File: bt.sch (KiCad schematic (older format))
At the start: 3 parts, among them J5 RN52_BREAKOUT, P1 CONN_01X06

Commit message: Add a line in module and use a smaller jack.
Lots of changes:
Added a line in. This requires another audio switch, so that's added to
the audio switch module.
Also, since I'm using two jacks, I chose a smaller jack module. This
needed a new footprint, and a new 3d model. The footprint is trickier,
since it really needed slots, which OSH won't guarantee. I've given it a
unique footprint to try to optimize the pad size around the edges of the
pins.
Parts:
- renumbered C4 to C3, J5 to J6
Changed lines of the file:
@@
 $Descr USLetter 11000 8500
 encoding utf-8
-Sheet 6 8
+Sheet 6 10
 Title "Blubaru"
 Date "2017-02-28"
@@
 $EndDescr
 $Comp
-L RN52_BREAKOUT J5
+L RN52_BREAKOUT J6
 U 1 1 589AA2F8
 P 5100 2950
-F 0 "J5" H 5100 850 60  0000 C CNN
+F 0 "J6" H 5100 850 60  0000 C CNN
 F 1 "RN52_BREAKOUT" H 5100 2950 60  0000 C CNN
 F 2 "blubaru:RN52_Breakout" H 5100 2950 60  0001 C CNN
@@
 NoConn ~ 5800 3950
 $Comp
-L C C4
+L C C3
 U 1 1 589BA198
 P 4250 5150
-F 0 "C4" H 4275 5250 50  0000 L CNN
+F 0 "C3" H 4275 5250 50  0000 L CNN
 F 1 "0.1uF" H 4275 5050 50  0000 L CNN
 F 2 "blubaru:C_Disc_D4.0mm_W2.6mm_P2.50mm" H 4288 5000 50  0001 C CNN
@@
 $EndSheet
 Text HLabel 8150 3050 2    60   Output ~ 0
-LineOutL
+BT_L
 Text HLabel 8150 3150 2    60   Output ~ 0
-LineOutR
+BT_R
 Wire Wire Line
 	7800 3050 8150 3050

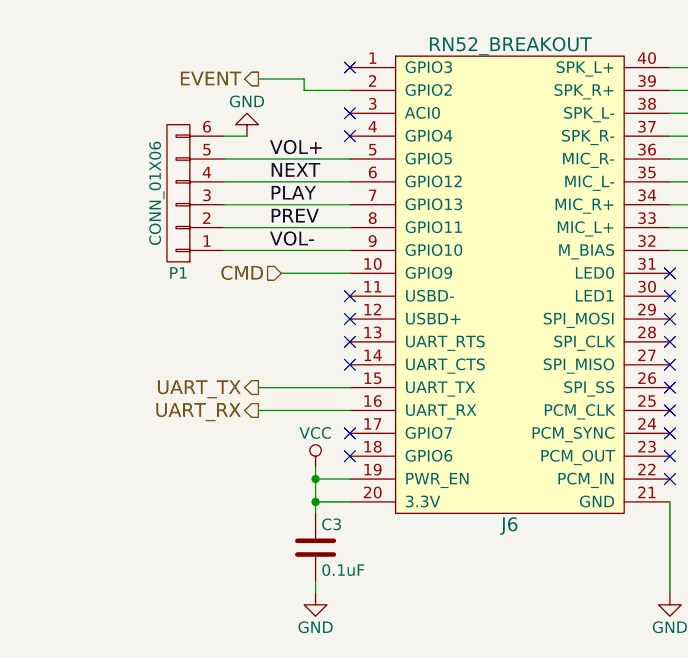
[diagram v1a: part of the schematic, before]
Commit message: Major update to use Atmel ATTINY4313
Replace Pro Micro as microcontroller. Mostly contianed within the
control sheet.
Moved LEDs all onto control sheet.
Updated a few capacitors.
Added a reset switch. Still need to decide part.
Updated a few capacitor models for 4.0.7
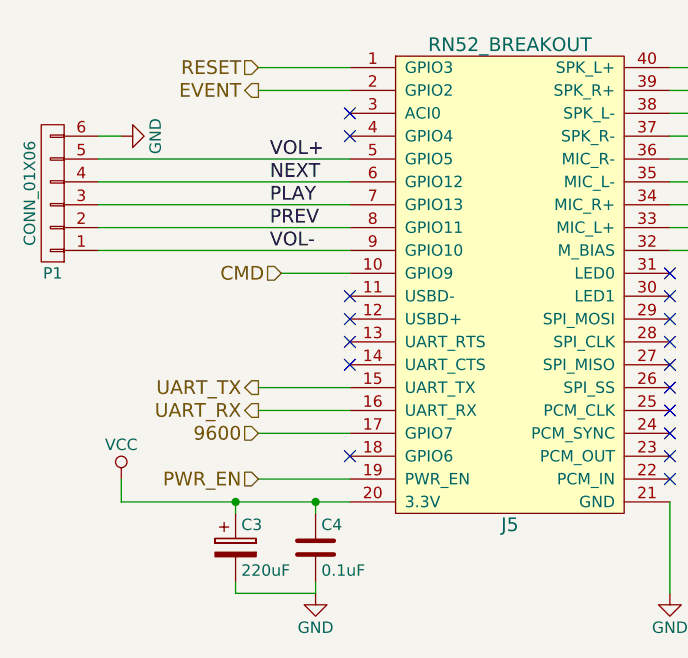
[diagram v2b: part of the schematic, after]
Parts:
- added C3: 220uF, blubaru:CP_Radial_D6.3mm_P2.50mm, symbol CP
- renumbered C3 to C4, J6 to J5
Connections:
- net GND: now also C3.2
- net VCC: now also C3.1; no longer J5.19 (PWR_EN)
- net RESET: now reaches J5.1 (GPIO3)
- net 9600: now reaches J5.17 (GPIO7)
- new net PWR_EN: J5.19 (PWR_EN)
- no-connect marks 19 -> 17
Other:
- moved on the sheet: P1
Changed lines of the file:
@@
 $Descr USLetter 11000 8500
 encoding utf-8
-Sheet 6 10
+Sheet 5 10
 Title "Blubaru"
 Date "2017-02-28"
@@
 $EndDescr
 $Comp
-L RN52_BREAKOUT J6
+L RN52_BREAKOUT J5
 U 1 1 589AA2F8
 P 5100 2950
-F 0 "J6" H 5100 850 60  0000 C CNN
+F 0 "J5" H 5100 850 60  0000 C CNN
 F 1 "RN52_BREAKOUT" H 5100 2950 60  0000 C CNN
 F 2 "blubaru:RN52_Breakout" H 5100 2950 60  0001 C CNN
@@
 $EndComp
 $Comp
-L GND #PWR022
+L GND #PWR017
 U 1 1 589AA392
 P 5800 5350
-F 0 "#PWR022" H 5800 5100 50  0001 C CNN
+F 0 "#PWR017" H 5800 5100 50  0001 C CNN
 F 1 "GND" H 5800 5200 50  0000 C CNN
 F 2 "" H 5800 5350 50  0000 C CNN
@@
 $EndComp
 $Comp
-L VCC #PWR023
+L VCC #PWR018
 U 1 1 589AA3E5
-P 4250 4800
-F 0 "#PWR023" H 4250 4650 50  0001 C CNN
-F 1 "VCC" H 4250 4950 50  0000 C CNN
-F 2 "" H 4250 4800 50  0000 C CNN
-F 3 "" H 4250 4800 50  0000 C CNN
-	1    4250 4800
-	1    0    0    -1
-$EndComp
-NoConn ~ 4400 3050
+P 3400 4850
+F 0 "#PWR018" H 3400 4700 50  0001 C CNN
+F 1 "VCC" H 3400 5000 50  0000 C CNN
+F 2 "" H 3400 4850 50  0000 C CNN
+F 3 "" H 3400 4850 50  0000 C CNN
+	1    3400 4850
+	1    0    0    -1
+$EndComp
 NoConn ~ 4400 3250
 NoConn ~ 4400 3350
@@
 NoConn ~ 4400 4250
 NoConn ~ 4400 4350
-NoConn ~ 4400 4650
 NoConn ~ 4400 4750
 NoConn ~ 5800 4850
@@
 NoConn ~ 5800 3950
 $Comp
-L C C3
+L C C4
 U 1 1 589BA198
 P 4250 5150
-F 0 "C3" H 4275 5250 50  0000 L CNN
+F 0 "C4" H 4275 5250 50  0000 L CNN
 F 1 "0.1uF" H 4275 5050 50  0000 L CNN
 F 2 "blubaru:C_Disc_D4.0mm_W2.6mm_P2.50mm" H 4288 5000 50  0001 C CNN
@@
 $EndComp
 Wire Wire Line
-	3850 3450 4400 3450
-Wire Wire Line
-	3850 3550 4400 3550
-Wire Wire Line
-	3850 3650 4400 3650
-Wire Wire Line
-	3850 3750 4400 3750
-Wire Wire Line
-	3850 3850 4400 3850
+	3300 3450 4400 3450
+Wire Wire Line
+	3300 3550 4400 3550
+Wire Wire Line
+	3300 3650 4400 3650
+Wire Wire Line
+	3300 3750 4400 3750
+Wire Wire Line
+	3300 3850 4400 3850
 Wire Wire Line
 	5800 4950 5800 5350
@@
 L CONN_01X06 P1
 U 1 1 589E7B79
-P 3650 3600
-F 0 "P1" H 3650 3950 50  0000 C CNN
-F 1 "CONN_01X06" V 3750 3600 50  0000 C CNN
-F 2 "Pin_Headers:Pin_Header_Straight_1x06_Pitch2.54mm" H 3650 3600 50  0001 C CNN
-F 3 "" H 3650 3600 50  0000 C CNN
-	1    3650 3600
+P 3100 3600
+F 0 "P1" H 3100 3950 50  0000 C CNN
+F 1 "CONN_01X06" V 3200 3600 50  0000 C CNN
+F 2 "Pin_Headers:Pin_Header_Straight_1x06_Pitch2.54mm" H 3100 3600 50  0001 C CNN
+F 3 "" H 3100 3600 50  0000 C CNN
+	1    3100 3600
 	-1   0    0    1
 $EndComp
 $Comp
-L GND #PWR024
+L GND #PWR019
 U 1 1 589E813D
-P 3950 3350
-F 0 "#PWR024" H 3950 3100 50  0001 C CNN
-F 1 "GND" H 3950 3200 50  0000 C CNN
-F 2 "" H 3950 3350 50  0000 C CNN
-F 3 "" H 3950 3350 50  0000 C CNN
-	1    3950 3350
-	-1   0    0    1
-$EndComp
-Wire Wire Line
-	3850 3350 3950 3350
+P 3400 3350
+F 0 "#PWR019" H 3400 3100 50  0001 C CNN
+F 1 "GND" H 3400 3200 50  0000 C CNN
+F 2 "" H 3400 3350 50  0000 C CNN
+F 3 "" H 3400 3350 50  0000 C CNN
+	1    3400 3350
+	0    -1   -1   0
+$EndComp
 Wire Wire Line
 	5800 3050 6700 3050
@@
 Text HLabel 4100 3950 0    60   Input ~ 0
 CMD
-Text HLabel 4000 3100 0    60   Output ~ 0
+Text HLabel 4000 3150 0    60   Output ~ 0
 EVENT
-Wire Wire Line
-	4000 3100 4200 3100
-Wire Wire Line
-	4200 3100 4200 3150
-Wire Wire Line
-	4200 3150 4400 3150
 Wire Wire Line
 	4100 3950 4400 3950
@@
 F7 "R+" I L 6700 3150 60
 $EndSheet
-Wire Wire Line
-	4400 4850 4250 4850
-Wire Wire Line
-	4250 4800 4250 5000
-Connection ~ 4250 4850
 Connection ~ 4250 4950
 Wire Wire Line
-	4250 4950 4400 4950
-$Comp
-L GND #PWR025
+	3400 4950 4400 4950
+$Comp
+L GND #PWR020
 U 1 1 594F3947
 P 4250 5350
-F 0 "#PWR025" H 4250 5100 50  0001 C CNN
+F 0 "#PWR020" H 4250 5100 50  0001 C CNN
 F 1 "GND" H 4250 5200 50  0000 C CNN
 F 2 "" H 4250 5350 50  0001 C CNN
@@
 Wire Wire Line
 	4250 5300 4250 5350
+$Comp
+L CP C3
+U 1 1 59F2DEF7
+P 3900 5150
+F 0 "C3" H 3925 5250 50  0000 L CNN
+F 1 "220uF" H 3925 5050 50  0000 L CNN
+F 2 "blubaru:CP_Radial_D6.3mm_P2.50mm" H 3938 5000 50  0001 C CNN
+F 3 "http://www.nichicon.co.jp/english/products/pdfs/e-usw.pdf" H 3900 5150 50  0001 C CNN
+	1    3900 5150
+	1    0    0    -1
+$EndComp
+Wire Wire Line
+	3900 5000 3900 4950
+Wire Wire Line
+	3900 5300 3900 5350
+Wire Wire Line
+	3900 5350 4250 5350
+Wire Wire Line
+	3400 4850 3400 4950
+Connection ~ 3900 4950
+Wire Wire Line
+	3300 3350 3400 3350
+Wire Wire Line
+	4400 4650 4000 4650
+Wire Wire Line
+	4400 4850 4000 4850
+Wire Wire Line
+	4400 3150 4000 3150
+Wire Wire Line
+	4400 3050 4000 3050
+Text HLabel 4000 3050 0    60   Input ~ 0
+RESET
+Text HLabel 4000 4650 0    60   Input ~ 0
+9600
+Text HLabel 4000 4850 0    60   Input ~ 0
+PWR_EN
+Wire Wire Line
+	4250 4950 4250 5000
 $EndSCHEMATC

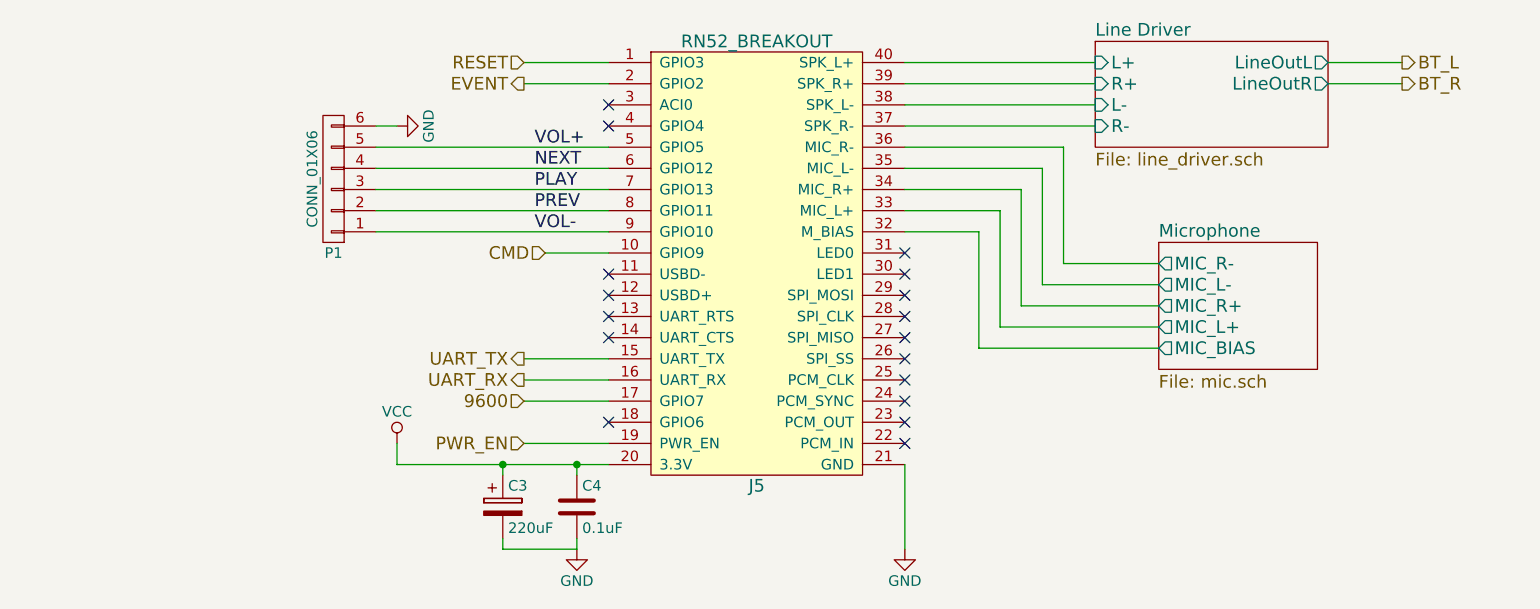
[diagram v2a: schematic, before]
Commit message: Add LEDs to BT module
These already exist on the breakout board, but they will be more visible
if I add resistors to the front panel. They can be removed if space is
limited and the case is translucent, but add them for now. In V2, there
won't be a breakout board, so adding them now makes the V1 to V2 fewer
changes.
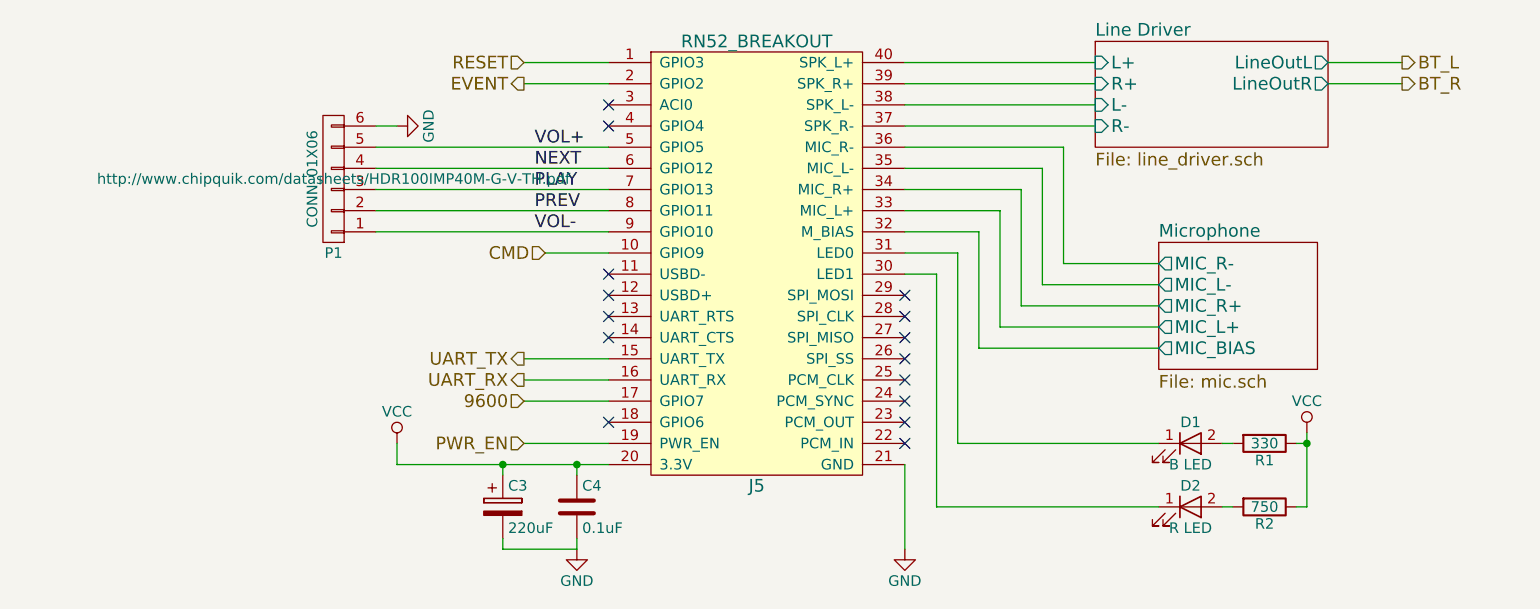
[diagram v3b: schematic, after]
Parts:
- added D1: B LED, LEDs:LED_D3.0mm_Horizontal_O1.27mm_Z6.0mm, symbol LED
- added D2: R LED, LEDs:LED_D3.0mm_Horizontal_O1.27mm_Z6.0mm, symbol LED
- added R1: 330, Resistors_THT:R_Axial_DIN0204_L3.6mm_D1.6mm_P5.08mm_Horizontal, symbol R
- added R2: 750, Resistors_THT:R_Axial_DIN0204_L3.6mm_D1.6mm_P5.08mm_Horizontal, symbol R
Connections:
- net VCC: now also R1.1, R2.1
- net at J5.30 (LED1): now also D2.1 (K)
- net at J5.31 (LED0): now also D1.1 (K)
- new net: D1.2 (A), R1.2
- new net: D2.2 (A), R2.2
- no-connect marks 17 -> 15
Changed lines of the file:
@@
 NoConn ~ 5800 4250
 NoConn ~ 5800 4150
-NoConn ~ 5800 4050
-NoConn ~ 5800 3950
 $Comp
 L C C4
@@
 F 1 "CONN_01X06" V 3200 3600 50  0000 C CNN
 F 2 "Pin_Headers:Pin_Header_Straight_1x06_Pitch2.54mm" H 3100 3600 50  0001 C CNN
-F 3 "" H 3100 3600 50  0000 C CNN
+F 3 "http://www.chipquik.com/datasheets/HDR100IMP40M-G-V-TH.pdf" H 3100 3600 50  0000 C CNN
 	1    3100 3600
 	-1   0    0    1
@@
 Wire Wire Line
 	4250 4950 4250 5000
+$Comp
+L LED D1
+U 1 1 5A165420
+P 7150 4850
+F 0 "D1" H 7150 4950 50  0000 C CNN
+F 1 "B LED" H 7150 4750 50  0000 C CNN
+F 2 "LEDs:LED_D3.0mm_Horizontal_O1.27mm_Z6.0mm" H 7150 4850 50  0001 C CNN
+F 3 "http://www.kingbrightusa.com/images/catalog/SPEC/WP710A10LVBC-D.pdf" H 7150 4850 50  0001 C CNN
+	1    7150 4850
+	1    0    0    -1
+$EndComp
+$Comp
+L LED D2
+U 1 1 5A16549D
+P 7150 5150
+F 0 "D2" H 7150 5250 50  0000 C CNN
+F 1 "R LED" H 7150 5050 50  0000 C CNN
+F 2 "LEDs:LED_D3.0mm_Horizontal_O1.27mm_Z6.0mm" H 7150 5150 50  0001 C CNN
+F 3 "http://www.kingbrightusa.com/images/catalog/SPEC/WP710A10LSECK-J3.pdf" H 7150 5150 50  0001 C CNN
+	1    7150 5150
+	1    0    0    -1
+$EndComp
+$Comp
+L R R1
+U 1 1 5A165502
+P 7500 4850
+F 0 "R1" V 7580 4850 50  0000 C CNN
+F 1 "330" V 7500 4850 50  0000 C CNN
+F 2 "Resistors_THT:R_Axial_DIN0204_L3.6mm_D1.6mm_P5.08mm_Horizontal" V 7430 4850 50  0001 C CNN
+F 3 "https://www.seielect.com/Catalog/SEI-CF_CFM.pdf" H 7500 4850 50  0001 C CNN
+	1    7500 4850
+	0    1    1    0
+$EndComp
+$Comp
+L R R2
+U 1 1 5A16556D
+P 7500 5150
+F 0 "R2" V 7580 5150 50  0000 C CNN
+F 1 "750" V 7500 5150 50  0000 C CNN
+F 2 "Resistors_THT:R_Axial_DIN0204_L3.6mm_D1.6mm_P5.08mm_Horizontal" V 7430 5150 50  0001 C CNN
+F 3 "https://www.seielect.com/Catalog/SEI-CF_CFM.pdf" H 7500 5150 50  0001 C CNN
+	1    7500 5150
+	0    1    1    0
+$EndComp
+Wire Wire Line
+	7300 4850 7350 4850
+Wire Wire Line
+	7300 5150 7350 5150
+$Comp
+L VCC #PWR021
+U 1 1 5A1658A5
+P 7700 4800
+F 0 "#PWR021" H 7700 4650 50  0001 C CNN
+F 1 "VCC" H 7700 4950 50  0000 C CNN
+F 2 "" H 7700 4800 50  0001 C CNN
+F 3 "" H 7700 4800 50  0001 C CNN
+	1    7700 4800
+	1    0    0    -1
+$EndComp
+Wire Wire Line
+	7700 4800 7700 5150
+Wire Wire Line
+	7700 5150 7650 5150
+Wire Wire Line
+	7650 4850 7700 4850
+Connection ~ 7700 4850
+Wire Wire Line
+	7000 4850 6050 4850
+Wire Wire Line
+	6050 4850 6050 3950
+Wire Wire Line
+	6050 3950 5800 3950
+Wire Wire Line
+	7000 5150 5950 5150
+Wire Wire Line
+	5950 5150 5950 4050
+Wire Wire Line
+	5950 4050 5800 4050
 $EndSCHEMATC

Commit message: Add footprints for LEDs and tactile switches
Also create an initial layout for fun.
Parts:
- D1, D2: footprint LEDs:LED_D3.0mm_Horizontal_O1.27mm_Z6.0mm -> blubaru:LED_D3.0mm_Horizontal_O1.27mm_Z6.0mm; Holder datasheet (none) -> https://www.bivar.com/portals/0/products/H-10XC-X.pdf
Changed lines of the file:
@@
 F 0 "D1" H 7150 4950 50  0000 C CNN
 F 1 "B LED" H 7150 4750 50  0000 C CNN
-F 2 "LEDs:LED_D3.0mm_Horizontal_O1.27mm_Z6.0mm" H 7150 4850 50  0001 C CNN
+F 2 "blubaru:LED_D3.0mm_Horizontal_O1.27mm_Z6.0mm" H 7150 4850 50  0001 C CNN
 F 3 "http://www.kingbrightusa.com/images/catalog/SPEC/WP710A10LVBC-D.pdf" H 7150 4850 50  0001 C CNN
+F 4 "https://www.bivar.com/portals/0/products/H-10XC-X.pdf" H 7150 4850 60  0001 C CNN "Holder datasheet"
 	1    7150 4850
 	1    0    0    -1
@@
 F 0 "D2" H 7150 5250 50  0000 C CNN
 F 1 "R LED" H 7150 5050 50  0000 C CNN
-F 2 "LEDs:LED_D3.0mm_Horizontal_O1.27mm_Z6.0mm" H 7150 5150 50  0001 C CNN
+F 2 "blubaru:LED_D3.0mm_Horizontal_O1.27mm_Z6.0mm" H 7150 5150 50  0001 C CNN
 F 3 "http://www.kingbrightusa.com/images/catalog/SPEC/WP710A10LSECK-J3.pdf" H 7150 5150 50  0001 C CNN
+F 4 "https://www.bivar.com/portals/0/products/H-10XC-X.pdf" H 7150 5150 60  0001 C CNN "Holder datasheet"
 	1    7150 5150
 	1    0    0    -1

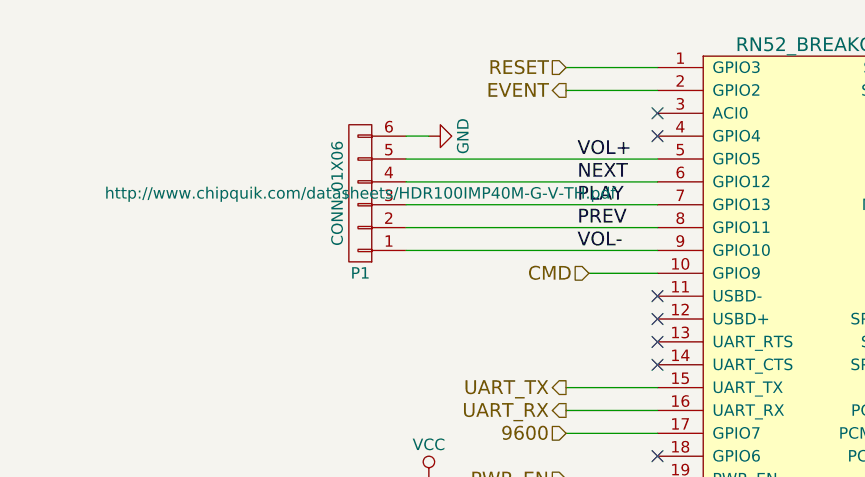
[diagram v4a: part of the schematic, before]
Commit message: Clean up some schematics for readability.
Run 12V from after power protection diode.
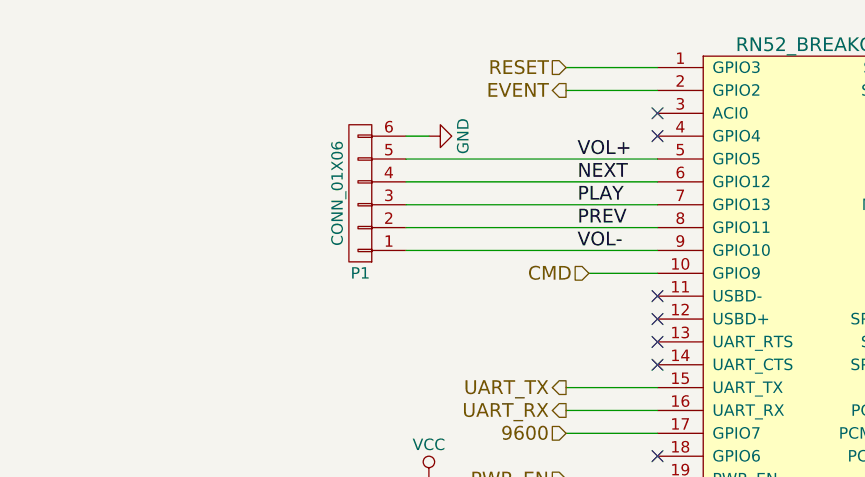
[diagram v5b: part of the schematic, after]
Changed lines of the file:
@@
 F 1 "CONN_01X06" V 3200 3600 50  0000 C CNN
 F 2 "Pin_Headers:Pin_Header_Straight_1x06_Pitch2.54mm" H 3100 3600 50  0001 C CNN
-F 3 "http://www.chipquik.com/datasheets/HDR100IMP40M-G-V-TH.pdf" H 3100 3600 50  0000 C CNN
+F 3 "http://www.chipquik.com/datasheets/HDR100IMP40M-G-V-TH.pdf" H 3100 3600 50  0001 C CNN
 	1    3100 3600
 	-1   0    0    1

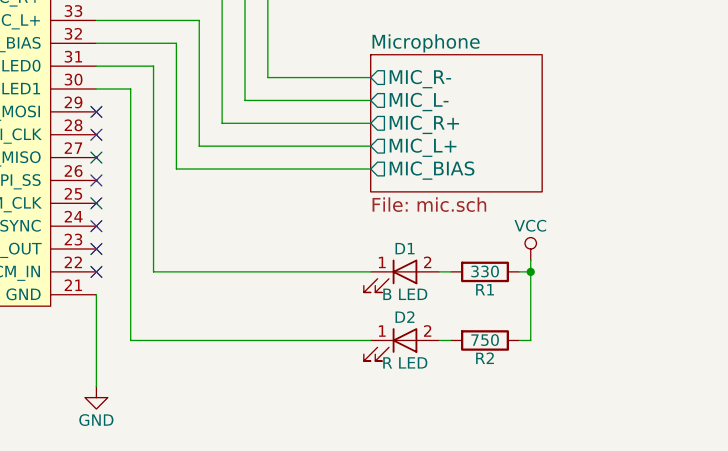
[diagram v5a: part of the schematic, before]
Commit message: Rename the bluetooth reset line
This is needed so it doesn't conflict with the MCU reset line of the
same name. Apparently that puts them on the same net.

Also, reorder the LEDs so they have nicer numbers on the board.
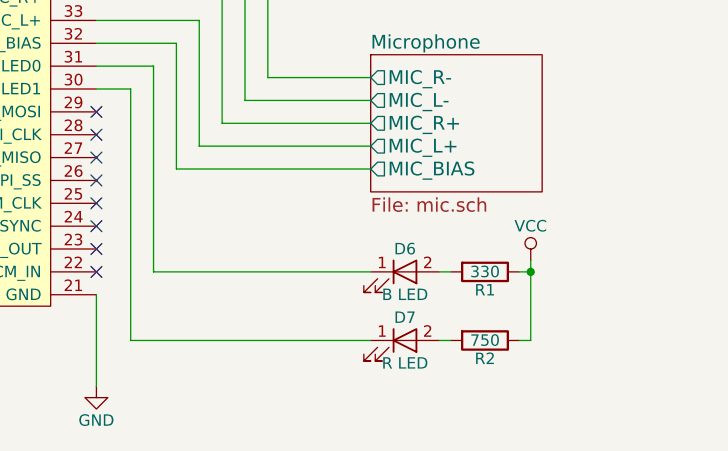
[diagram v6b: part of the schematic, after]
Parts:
- renumbered D1 to D6, D2 to D7
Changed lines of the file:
@@
 	4250 4950 4250 5000
 $Comp
-L LED D1
+L LED D6
 U 1 1 5A165420
 P 7150 4850
-F 0 "D1" H 7150 4950 50  0000 C CNN
+F 0 "D6" H 7150 4950 50  0000 C CNN
 F 1 "B LED" H 7150 4750 50  0000 C CNN
 F 2 "blubaru:LED_D3.0mm_Horizontal_O1.27mm_Z6.0mm" H 7150 4850 50  0001 C CNN
@@
 $EndComp
 $Comp
-L LED D2
+L LED D7
 U 1 1 5A16549D
 P 7150 5150
-F 0 "D2" H 7150 5250 50  0000 C CNN
+F 0 "D7" H 7150 5250 50  0000 C CNN
 F 1 "R LED" H 7150 5050 50  0000 C CNN
 F 2 "blubaru:LED_D3.0mm_Horizontal_O1.27mm_Z6.0mm" H 7150 5150 50  0001 C CNN
